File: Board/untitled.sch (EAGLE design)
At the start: 48 parts, among them IC2 MEGA16-A, Q1 8 MHz

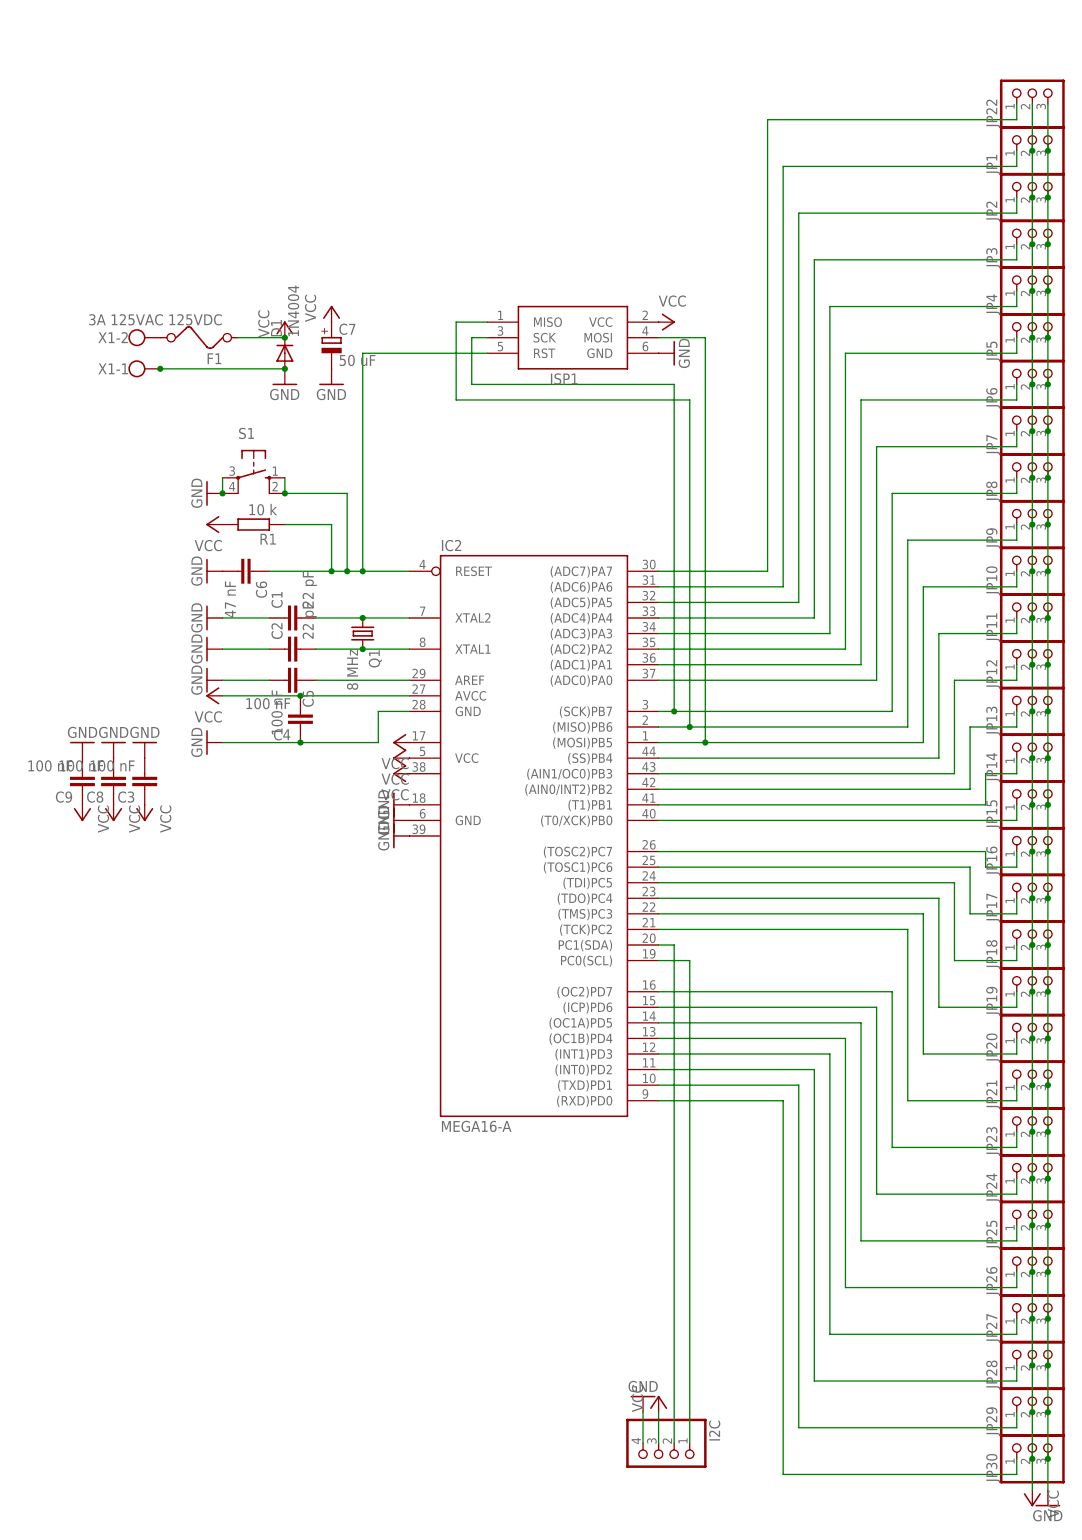
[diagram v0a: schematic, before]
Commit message: Seperate power input fot uC and servos. Change uC rom QFP to DIP for better repair process.
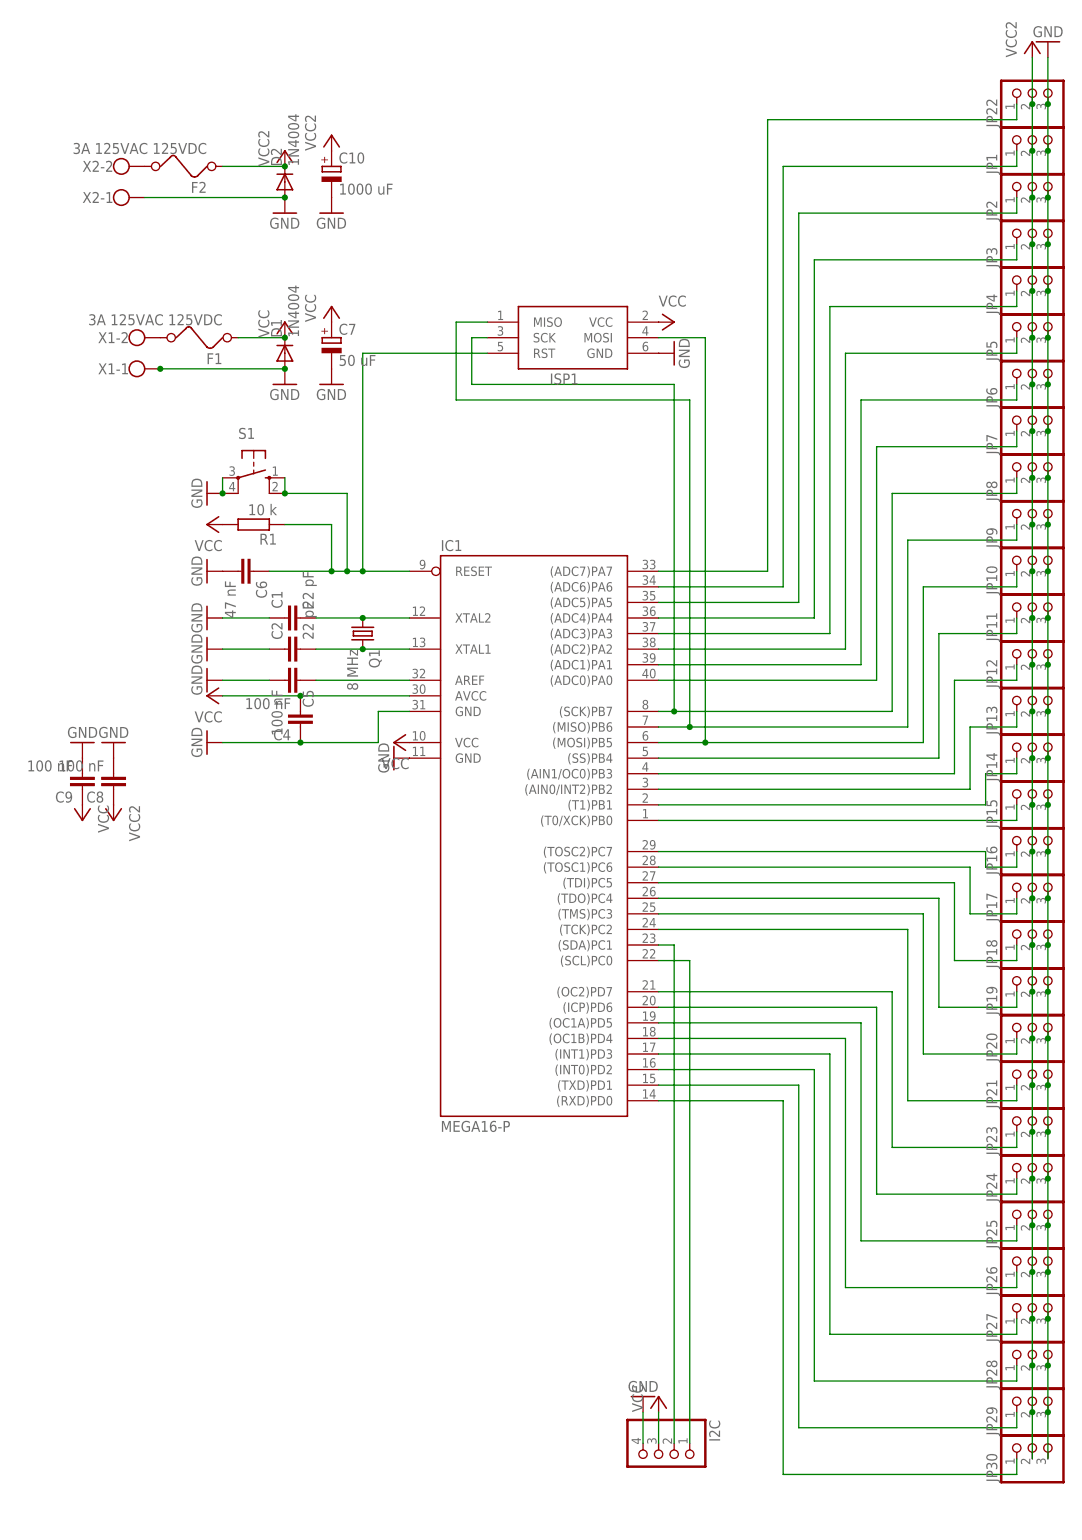
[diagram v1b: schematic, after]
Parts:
- removed C3: 100 nF, rcl:C-EUC0805
- removed IC2: MEGA16-A, atmel:MEGA16-A
- added C10: 1000 uF, rcl:CPOL-EUE2-5
- added D2: 1N4004, diode:DIODE-DO214AC
- added F2: 3A 125VAC 125VDC, special:FUSE
- added IC1: MEGA16-P, atmel:MEGA16-P
- added X2: (no value), con-wago-500:W237-102
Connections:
- new net N$9: F2.2, X2-2.KL
- net GND: now also C10.-, D2.A, IC1.GND, IC1.GND@1, X2-1.KL; no longer C3.2, IC2.GND, IC2.GND1, IC2.GND2, IC2.GND@1
- net N$1: now also IC1.XTAL2; no longer IC2.XTAL2
- net N$13: now also IC1.(ADC4)PA4; no longer IC2.(ADC4)PA4
- net N$15: now also IC1.(ADC7)PA7; no longer IC2.(ADC7)PA7
- net N$16: now also IC1.(ADC1)PA1; no longer IC2.(ADC1)PA1
- net N$2: now also IC1.XTAL1; no longer IC2.XTAL1
- net N$21: now also IC1.(TOSC1)PC6; no longer IC2.(TOSC1)PC6
- net N$22: now also IC1.(MISO)PB6; no longer IC2.(MISO)PB6
- net N$23: now also IC1.(TDI)PC5; no longer IC2.(TDI)PC5
- net N$24: now also IC1.(ADC0)PA0; no longer IC2.(ADC0)PA0
- net N$25: now also IC1.(AIN1/OC0)PB3; no longer IC2.(AIN1/OC0)PB3
- net N$27: now also IC1.(TOSC2)PC7; no longer IC2.(TOSC2)PC7
- net N$29: now also IC1.(T1)PB1; no longer IC2.(T1)PB1
- net N$3: now also IC1.AREF; no longer IC2.AREF
- net N$30: now also IC1.(AIN0/INT2)PB2; no longer IC2.(AIN0/INT2)PB2
- net N$31: now also IC1.(ADC3)PA3; no longer IC2.(ADC3)PA3
- net N$32: now also IC1.(SS)PB4; no longer IC2.(SS)PB4
- net N$33: now also IC1.(SDA)PC1; no longer IC2.PC1(SDA)
- net N$34: now also IC1.(SCL)PC0; no longer IC2.PC0(SCL)
- net N$36: now also IC1.(ADC2)PA2; no longer IC2.(ADC2)PA2
- net N$39: now also IC1.(ADC5)PA5; no longer IC2.(ADC5)PA5
- net N$40: now also IC1.(ADC6)PA6; no longer IC2.(ADC6)PA6
- net N$41: now also IC1.(TDO)PC4; no longer IC2.(TDO)PC4
- net N$42: now also IC1.(TMS)PC3; no longer IC2.(TMS)PC3
- net N$43: now also IC1.(TCK)PC2; no longer IC2.(TCK)PC2
- net N$44: now also IC1.(OC2)PD7; no longer IC2.(OC2)PD7
- net N$45: now also IC1.(ICP)PD6; no longer IC2.(ICP)PD6
- net N$46: now also IC1.(OC1A)PD5; no longer IC2.(OC1A)PD5
- net N$47: now also IC1.(OC1B)PD4; no longer IC2.(OC1B)PD4
- net N$48: now also IC1.(INT1)PD3; no longer IC2.(INT1)PD3
- net N$49: now also IC1.(INT0)PD2; no longer IC2.(INT0)PD2
- net N$5: now also IC1.(SCK)PB7; no longer IC2.(SCK)PB7
- net N$56: now also IC1.(TXD)PD1; no longer IC2.(TXD)PD1
- net N$57: now also IC1.(RXD)PD0; no longer IC2.(RXD)PD0
- net N$6: now also IC1.(MOSI)PB5; no longer IC2.(MOSI)PB5
- net N$7: now also IC1.RESET; no longer IC2.RESET
- net N$8: now also IC1.(T0/XCK)PB0; no longer IC2.(T0/XCK)PB0
- net VCC: now also C10.+, D2.C, F2.1, IC1.AVCC, IC1.VCC; no longer C3.1, IC2.AVCC, IC2.VCC, IC2.VCC1, IC2.VCC2

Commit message: Create new board
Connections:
- removed net N$33: I2C.2, IC1.(SDA)PC1
- removed net N$34: I2C.1, IC1.(SCL)PC0
- new net +5V: C10.+, C8.2, D2.C, F2.1, JP1.2, JP10.2, JP11.2, JP12.2, JP13.2, JP14.2, JP15.2, JP16.2, JP17.2, JP18.2, JP19.2, JP2.2, JP20.2, JP21.2, JP22.2, JP23.2, JP24.2, JP25.2, JP26.2, JP27.2, JP28.2, JP29.2, JP3.2, JP30.2, JP4.2, JP5.2, JP6.2, JP7.2, JP8.2, JP9.2
- new net N$10: F2.2, X2-1.KL
- new net N$17: I2C.3, IC1.(SDA)PC1
- net GND: now also C8.1, C9.1, I2C.1, X2-2.KL; no longer C8.2, C9.2, I2C.4, X2-1.KL
- net N$9: now also I2C.4, IC1.(SCL)PC0; no longer F2.2, X2-2.KL
- net VCC: now also C9.2, I2C.2; no longer C10.+, C8.1, C9.1, D2.C, F2.1, I2C.3, JP1.2, JP10.2, JP11.2, JP12.2, JP13.2, JP14.2, JP15.2, JP16.2, JP17.2, JP18.2, JP19.2, JP2.2, JP20.2, JP21.2, JP22.2, JP23.2, JP24.2, JP25.2, JP26.2, JP27.2, JP28.2, JP29.2, JP3.2, JP30.2, JP4.2, JP5.2, JP6.2, JP7.2, JP8.2, JP9.2
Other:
- moved on the sheet: I2C, X1-1, X1-2, X2-1, X2-2
